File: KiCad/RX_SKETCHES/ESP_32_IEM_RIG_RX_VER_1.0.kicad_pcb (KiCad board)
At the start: 2 copper layers, 64 parts, among them J1 AudioJack3, J6 USB_C_Receptacle_USB2.0_16P, Q1 S8050, Q2 S8050, SW2 Interpolation Mode, SW3 DAC Soft Mute, SW4 ON/OFF, U1 PCM5102, U2 ESP32-WROOM-32U, U3 MAX97220AETE_T, U4 LM3940IMPX-3.3_NOPB, U5 CP2102C-Axx-xQFN24

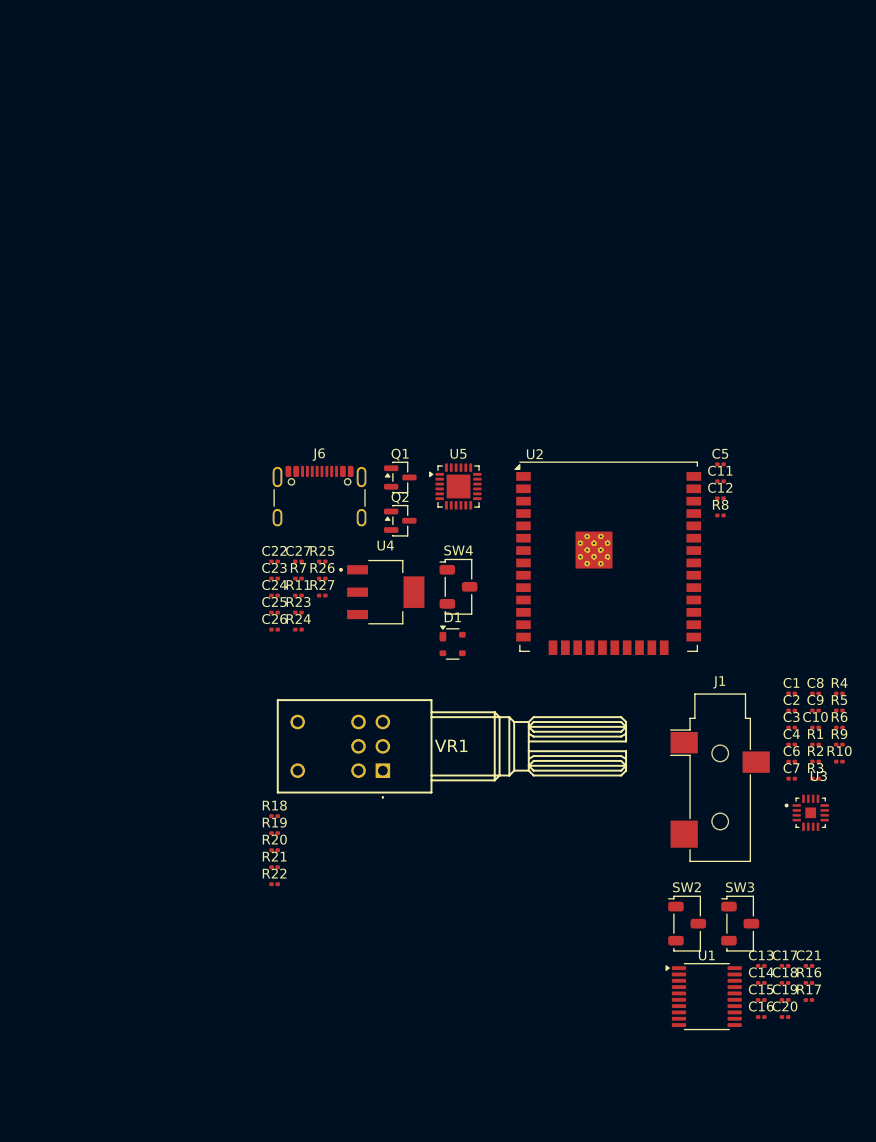
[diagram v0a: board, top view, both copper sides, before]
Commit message: RX: finish layout, retune gain/coupling, move ESD clamp to unswitched VBUS
Board now passes DRC with zero unconnected items and zero schematic-parity
issues. Remaining 16 violations are footprint-inherent (ESP32 module thermal
via array at 0.2 mm drill, USB-C NPTH-to-pad spacing) and are documented
rather than routed around.

Analog changes, with the reasoning captured in README.org and
docs/hardware_revisions.org so the numbers can be re-checked:

- Gain network populated at RF 4.7k / RIN 47k (-20 dB) instead of DNP 10k.
  Tames the DAC's 2.1 Vrms into sensitive IEMs, unloads the pot taper, and
  moves the coupling corner out of the audible band.
- Coupling caps C1-C4 0.47uF -> 1uF. Corner 7.2 Hz -> 3.4 Hz, and it halves
  the signal developed across the ceramic at 20 Hz, cutting Class-II
  dielectric distortion where it actually occurs.
- D1's third TVS channel moved off the switched +5V rail onto VBUS_RAW. The
  clamp has to sit on the connector pin that is exposed to a finger; behind
  the power switch it went open exactly when the board is most handled.
- SW3 soft mute: XSMT_SEL moved to the throw that puts mute on the south
  slide position. All three switches now follow one rule -- the open throw
  is the safe default (off / quality filter / muted).
- PCM5102 mode pins no longer float: FLT and XSMT get 100k pulldowns, DEMP
  and FMT strap to GND.
- C28 and the four mounting holes added to the schematic to clear parity
  errors against parts that only existed on the PCB.

Also adds a .gitignore so the 24 MB editor .history/ directory and ESP-IDF
build output stop showing up as untracked.

Co-authored-by: Cursor <cursoragent@cursor.com>
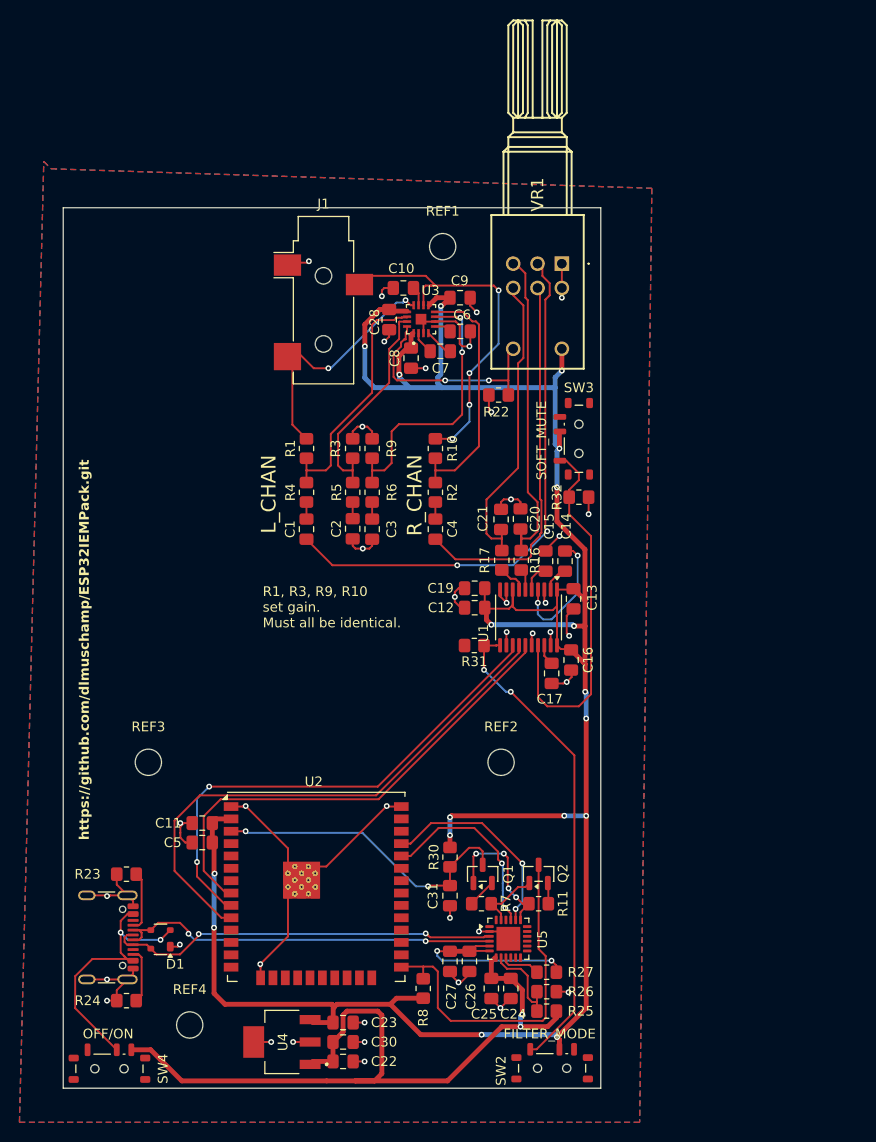
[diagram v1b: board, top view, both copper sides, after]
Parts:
- removed C18: 10u, Capacitor_SMD:C_0805_2012Metric_Pad1.15x1.40mm_HandSolder
- removed R18, R20: 1k, Resistor_SMD:R_0805_2012Metric_Pad1.20x1.40mm_HandSolder
- removed R19, R21: 10R, Resistor_SMD:R_0805_2012Metric_Pad1.20x1.40mm_HandSolder
- added C28: 1u, Capacitor_SMD:C_0805_2012Metric_Pad1.18x1.45mm_HandSolder, F.Cu at (130.0, 50.0)
- added C30: 22u, Capacitor_SMD:C_0805_2012Metric_Pad1.18x1.45mm_HandSolder, F.Cu at (125.3, 124.2)
- added C31: 0.1u, Capacitor_SMD:C_0805_2012Metric_Pad1.18x1.45mm_HandSolder, F.Cu at (136.2, 109.2)
- added R30: 10k, Resistor_SMD:R_0805_2012Metric_Pad1.20x1.40mm_HandSolder, F.Cu at (136.2, 105.2)
- added R31: 100k, Resistor_SMD:R_0805_2012Metric_Pad1.20x1.40mm_HandSolder, F.Cu at (138.8, 83.5)
- added R32: 100k, Resistor_SMD:R_0805_2012Metric_Pad1.20x1.40mm_HandSolder, F.Cu at (149.5, 68.2)
- added REF1: MountingHole_2.7mm_M2.5, MountingHole:MountingHole_2.7mm_M2.5, F.Cu at (135.5, 42.5)
- added REF2: MountingHole_2.7mm_M2.5, MountingHole:MountingHole_2.7mm_M2.5, F.Cu at (141.5, 95.5)
- added REF3: MountingHole_2.7mm_M2.5, MountingHole:MountingHole_2.7mm_M2.5, F.Cu at (105.2, 95.5)
- added REF4: MountingHole_2.7mm_M2.5, MountingHole:MountingHole_2.7mm_M2.5, F.Cu at (109.5, 122.5)
- C1, C2, C3, C4: value 0.47u -> 1u; footprint Capacitor_SMD:C_0805_2012Metric_Pad1.15x1.40mm_HandSolder -> Capacitor_SMD:C_0805_2012Metric_Pad1.18x1.45mm_HandSolder
- C10, C11, C13, C14, C15, C16, C17, C19, C20, C21, C23, C24, C25, C26, C27, C6, C7, C8, C9: footprint Capacitor_SMD:C_0805_2012Metric_Pad1.15x1.40mm_HandSolder -> Capacitor_SMD:C_0805_2012Metric_Pad1.18x1.45mm_HandSolder
- C12: value 1u -> 10u; footprint Capacitor_SMD:C_0805_2012Metric_Pad1.15x1.40mm_HandSolder -> Capacitor_SMD:C_0805_2012Metric_Pad1.18x1.45mm_HandSolder
- C22: value 22u -> 0.47u; footprint Capacitor_SMD:C_0805_2012Metric_Pad1.15x1.40mm_HandSolder -> Capacitor_SMD:C_0805_2012Metric_Pad1.18x1.45mm_HandSolder
- C5: value 10u -> 22u; footprint Capacitor_SMD:C_0805_2012Metric_Pad1.15x1.40mm_HandSolder -> Capacitor_SMD:C_0805_2012Metric_Pad1.18x1.45mm_HandSolder
- R1, R10, R3, R9: value 10k -> 4.7k
- R2, R4, R5, R6: value 10k -> 47k
- SW2: value Interpolation Mode -> FILTER_MODE; footprint Button_Switch_SMD:Nidec_Copal_CAS-120A -> Button_Switch_SMD:SW_SPDT_Shouhan_MSK12C02
- SW3: value DAC Soft Mute -> SOFT_MUTE; footprint Button_Switch_SMD:Nidec_Copal_CAS-120A -> Button_Switch_SMD:SW_SPDT_Shouhan_MSK12C02
- SW4: footprint Button_Switch_SMD:Nidec_Copal_CAS-120A -> Button_Switch_SMD:SW_SPDT_Shouhan_MSK12C02
- moved C5 65.9 mm to (110.8, 103.8), turned to 180 degrees
- moved U3 64.6 mm to (133.3, 50.0), turned to 90 degrees
- moved J1 63.8 mm to (123.2, 48.0)
- moved C11 63.8 mm to (110.8, 101.8), turned to 180 degrees
- moved C10 61.9 mm to (131.5, 46.8), turned to 180 degrees
- moved SW4 61.2 mm to (101.2, 127.0)
- moved R1 60.5 mm to (121.5, 63.2), turned to 90 degrees
- moved R4 58.6 mm to (121.5, 67.8), turned to 90 degrees
- moved R3 58.4 mm to (126.2, 63.2), turned to 90 degrees
- moved C20 58.0 mm to (143.5, 70.5), turned to 90 degrees
- moved R8 57.4 mm to (133.5, 118.8), turned to 90 degrees
- moved C7 56.9 mm to (135.2, 53.2)
- moved R9 56.9 mm to (128.2, 63.2), turned to -90 degrees
- moved C9 56.0 mm to (137.3, 47.8)
- moved C6 55.8 mm to (137.3, 51.2)
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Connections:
- net /Amp/AMP_OUT_L renamed Net-(U3-OUTL)
- net /Amp/AMP_OUT_R renamed Net-(U3-OUTR)
- net /DAC/DIN renamed /DAC/DOUT
- net Net-(SW2-C) renamed /DAC/FLT_SEL
- C12 pad 1: GND -> +3V3
- C12 pad 2: /ESP Reciever/ESP_EN -> GND
- D1 pad 2: +5V -> /Power Management/VBUS_RAW
- J6 pad A4: Net-(SW4-B) -> /Power Management/VBUS_RAW
- J6 pad A9: Net-(SW4-B) -> /Power Management/VBUS_RAW
- J6 pad B4: Net-(SW4-B) -> /Power Management/VBUS_RAW
- J6 pad B9: Net-(SW4-B) -> /Power Management/VBUS_RAW
- R8 pad 2: /ESP Reciever/ESP_EN -> /ESP Reciever/ESP_IO0
- SW3 pad 1: unconnected-(SW3-C-Pad1) -> /DAC/XSMT_SEL
- SW3 pad 3: Net-(SW3-A) -> unconnected-(SW3-A-Pad3)
- SW4 pad 2: Net-(SW4-B) -> /Power Management/VBUS_RAW
- U1 pad 10: unconnected-(U1-DEMP-Pad10) -> GND
- U1 pad 16: unconnected-(U1-FMT-Pad16) -> GND
- U1 pad 17: Net-(SW3-A) -> /DAC/XSMT_SEL
- U2 pad 2: GND -> +3V3
- VR1 pad 3: /Volume Control/PRE_POT_IN_L -> /DAC/DAC_OUT_L
- VR1 pad 6: /Volume Control/PRE_POT_IN_R -> /DAC/DAC_OUT_R
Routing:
- net +3V3: track 0.00 -> 249.3 mm, vias 0 -> 18
- net GND: track 0.00 -> 129.9 mm, vias 0 -> 39
- net +5V: track 0.00 -> 79.3 mm, vias 0 -> 2
- net /DAC/DOUT: track 0.00 -> 56.3 mm
- net /Amp/POST_POT_IN_L: track 0.00 -> 55.8 mm, vias 0 -> 2
- net /DAC/BCK: track 0.00 -> 52.1 mm, vias 0 -> 2
- net /DAC/LRCLK: track 0.00 -> 50.1 mm
- net /DAC/FLT_SEL: track 0.00 -> 49.6 mm, vias 0 -> 2
- net Net-(U5-D+): track 0.00 -> 40.8 mm, vias 0 -> 2
- net Net-(U5-D-): track 0.00 -> 40.4 mm, vias 0 -> 2
- net /Amp/POST_POT_IN_R: track 0.00 -> 39.2 mm
- net /DAC/XSMT_SEL: track 0.00 -> 38.2 mm
- net Net-(U3-OUTR): track 0.00 -> 37.3 mm, vias 0 -> 4
- net /ESP Reciever/ESP_IO0: track 0.00 -> 36.9 mm
- net /DAC/DAC_OUT_L: track 0.00 -> 34.8 mm
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- added copper zone on B.Cu, net GND
- added copper zone on F.Cu, net GND
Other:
- board outline added: 55.2 x 90.5 mm
- board text added: "FILTER_MODE"
- board text added: "L_CHAN"
- board text added: "OFF/ON"
- board text added: "R1, R3, R9, R10 set gain. Must all be identical."
- board text added: "R10"
- board text added: "R_CHAN"
- board text added: "SOFT_MUTE"
- board text added: "https://github.com/dlmuschamp/ESP32IEMPack.git"

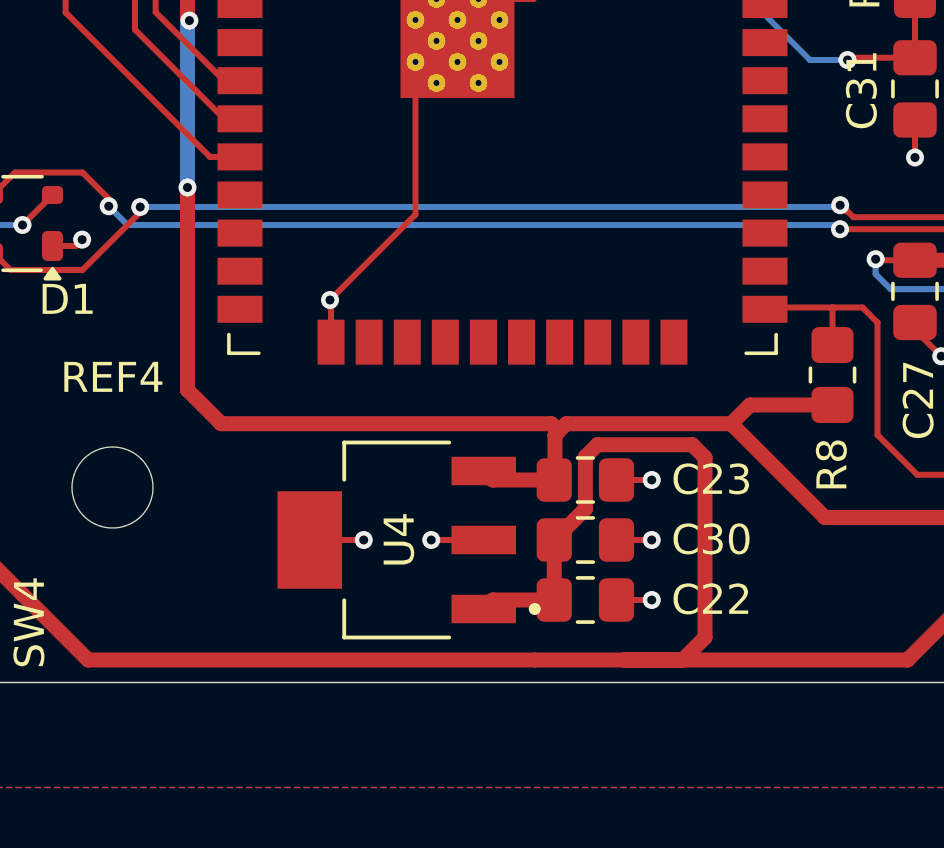
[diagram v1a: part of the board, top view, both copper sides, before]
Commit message: RX v1: map JLCPCB parts, fix LM3940 bulk cap, add production export
Retune the LM3940 input divider to 22k/47k and swap C23 to an EIA-3528
tantalum so the regulator meets its minimum ESR and stays stable.

Every SMT part now carries an LCSC number in the plugin's project.db, with
the ESP32 module and the mechanical/reference parts excluded from assembly
so the order stays on Economic pricing. Includes the generated Gerbers,
BOM, and CPL, plus the clean DRC/ERC reports.

Co-authored-by: Cursor <cursoragent@cursor.com>
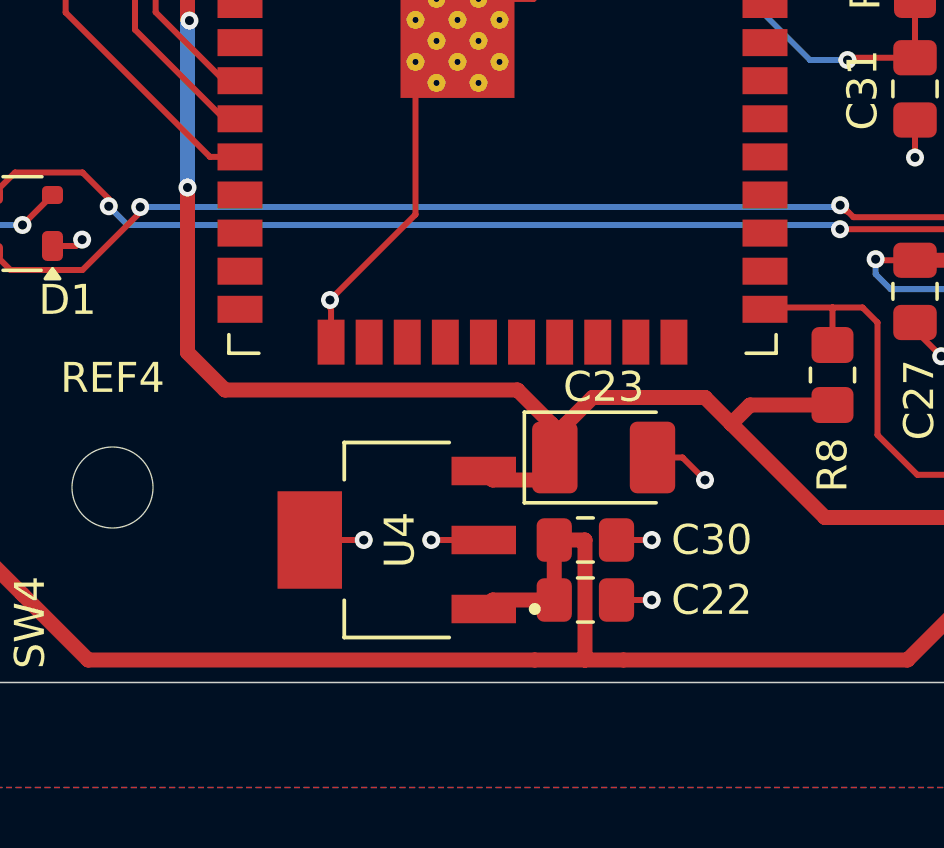
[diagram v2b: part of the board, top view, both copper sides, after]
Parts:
- C23: footprint Capacitor_SMD:C_0805_2012Metric_Pad1.18x1.45mm_HandSolder -> Capacitor_Tantalum_SMD:CP_EIA-3528-12_Kemet-T_HandSolder
- R25: value 22.1k -> 22k
- R26: value 47.5k -> 47k
- moved C23 0.97 mm to (125.9, 121.5)
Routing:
- net +5V: track 79.3 -> 67.8 mm
- net GND: track 129.9 -> 130.7 mm
